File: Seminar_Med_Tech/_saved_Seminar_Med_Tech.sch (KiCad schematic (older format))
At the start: 72 parts, among them J1 CONN_02X08, U1 JP22, U10 JP31, U11 JP32, U12 JP33, U13 JP34, U14 J5, U15 JP35, U16 JP36, U17 JP37, U18 ADS1298, U19 OPA2340, U2 JP23, U20 ADS1298, U3 JP24, U4 JP25, U5 JP26, U6 JP27, U7 JP28, U8 JP29, U9 JP30

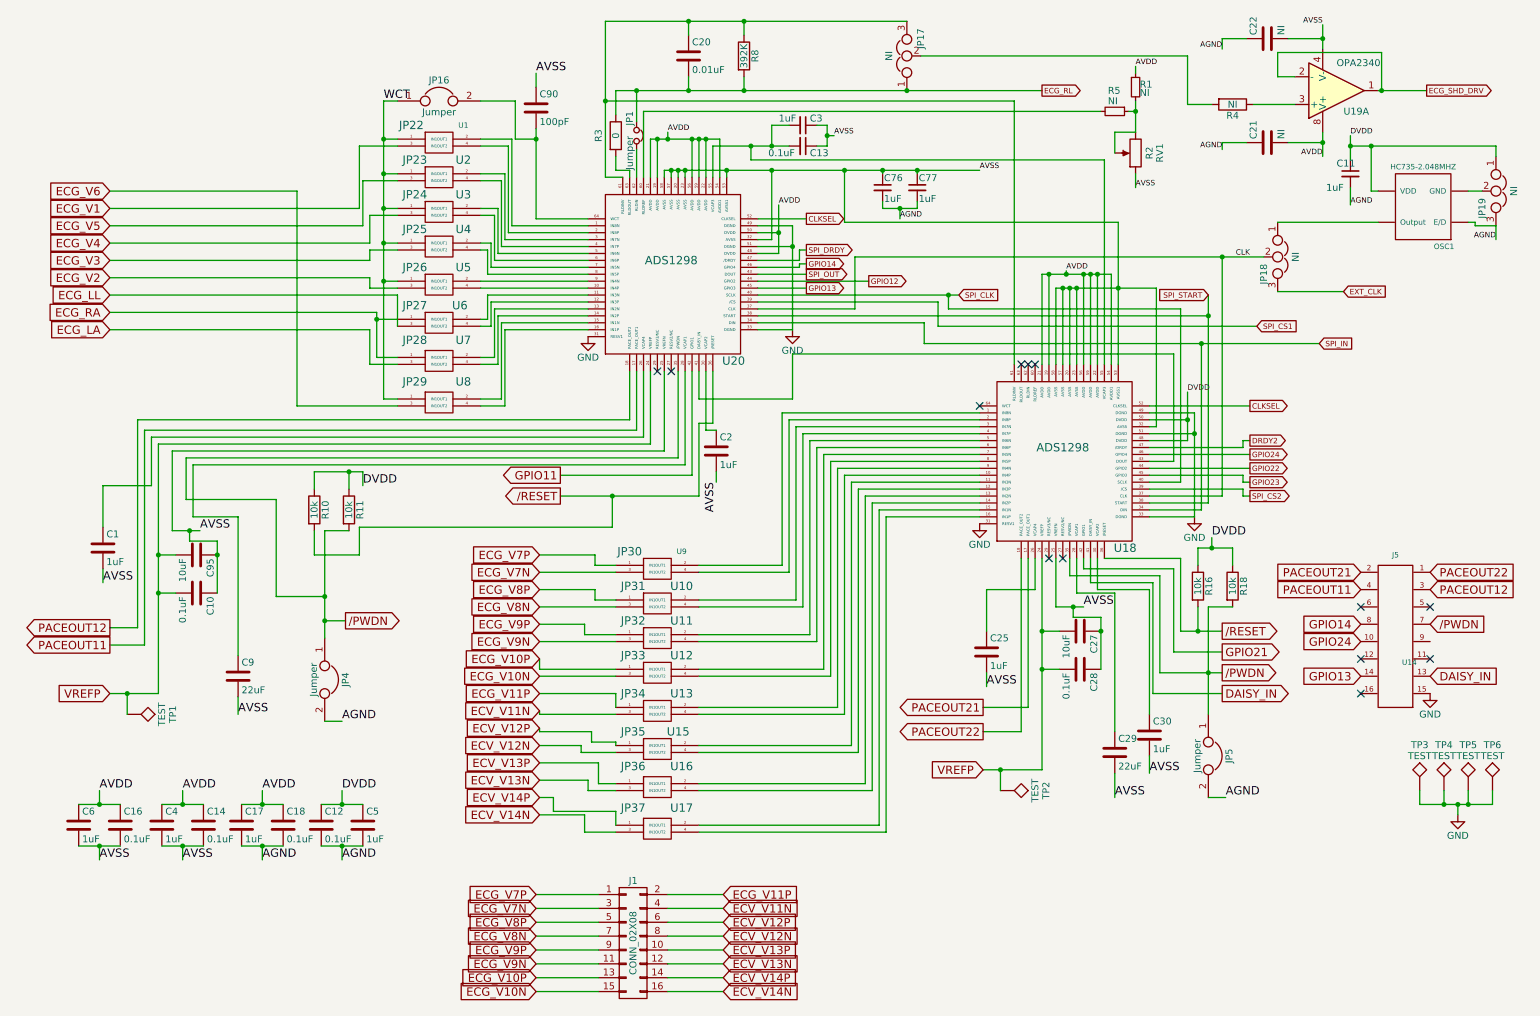
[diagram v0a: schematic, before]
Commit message: Changed labels
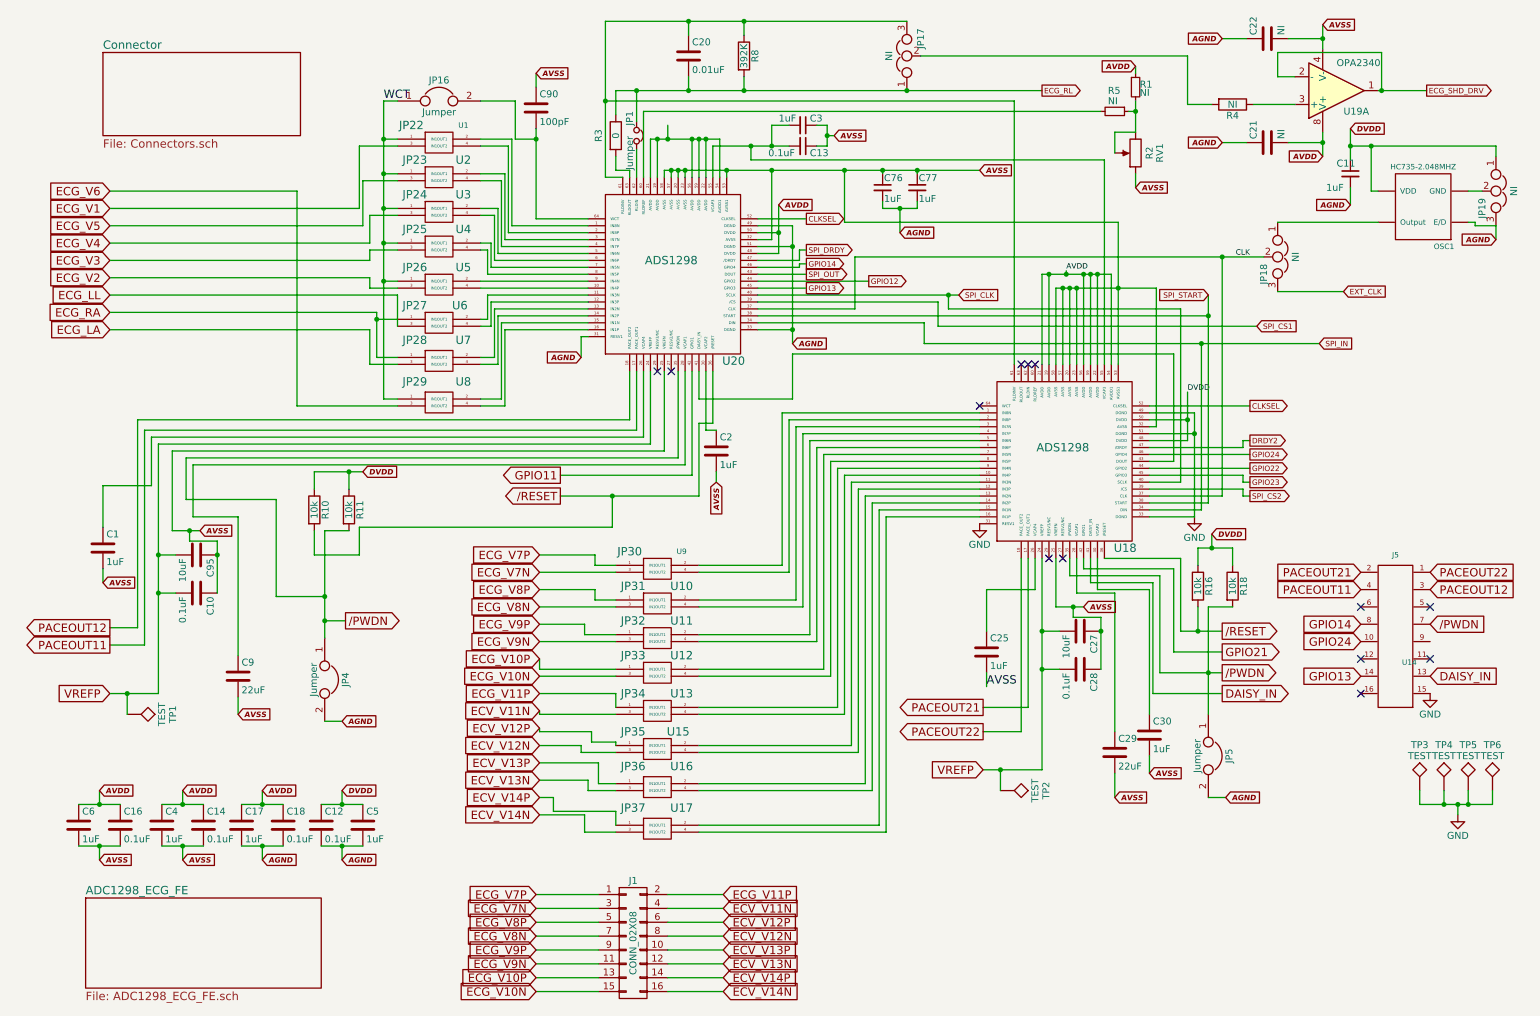
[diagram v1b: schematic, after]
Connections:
- net AGND: now also U20.31 (RESV1), U20.33 (DGND), U20.49 (DGND), U20.51 (DGND)
- net AVDD: no longer U20.19 (AVDD), U20.21 (AVDD), U20.22 (AVDD), U20.54 (AVDD1), U20.56 (AVDD), U20.59 (AVDD)
- net GND: no longer U20.31 (RESV1), U20.33 (DGND), U20.49 (DGND), U20.51 (DGND)
- new net: U20.19 (AVDD), U20.21 (AVDD), U20.22 (AVDD), U20.54 (AVDD1), U20.56 (AVDD), U20.59 (AVDD)
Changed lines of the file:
@@
 $Descr A4 11693 8268
 encoding utf-8
-Sheet 1 1
+Sheet 1 3
 Title ""
 Date ""
@@
 	1    0    0    -1
 $EndComp
-Text Label 4150 975  0    60   ~ 0
-AVSS
 $Comp
 L ADS1298 U20
@@
 Text Label 9300 2300 2    39   ~ 0
 CLK
-$Comp
-L GND #PWR02
-U 1 1 592AF0AE
-P 4525 2875
-F 0 "#PWR02" H 4525 2625 50  0001 C CNN
-F 1 "GND" H 4525 2725 50  0000 C CNN
-F 2 "" H 4525 2875 50  0001 C CNN
-F 3 "" H 4525 2875 50  0001 C CNN
-	1    4525 2875
-	1    0    0    -1
-$EndComp
 Text GLabel 7375 6000 0    60   Input ~ 0
 VREFP
@@
 	0    1    1    0
 $EndComp
-Text Label 9025 4325 0    60   ~ 0
-DVDD
 $Comp
 L C C30
@@
 	1    0    0    -1
 $EndComp
-Text Label 8575 6025 0    60   ~ 0
-AVSS
 $Comp
 L C C29
@@
 	1    0    0    -1
 $EndComp
-Text Label 8325 6200 0    60   ~ 0
-AVSS
 $Comp
 L C C25
@@
 $EndComp
 Text Label 7400 5400 0    60   ~ 0
-AVSS
-Text Label 8100 4825 0    60   ~ 0
 AVSS
 $Comp
@@
 	1    0    0    -1
 $EndComp
-Text Label 5450 3925 3    60   ~ 0
-AVSS
 $Comp
 L C C9
@@
 	1    0    0    -1
 $EndComp
-Text Label 2000 5600 0    60   ~ 0
-AVSS
 $Comp
 L C C1
@@
 	1    0    0    -1
 $EndComp
-Text Label 1025 4650 0    60   ~ 0
-AVSS
-Text Label 1725 4275 0    60   ~ 0
-AVSS
 $Comp
 L TEST TP1
@@
 	0    1    1    0
 $EndComp
-Text Label 2900 3950 0    60   ~ 0
-DVDD
 NoConn ~ 5025 3125
 NoConn ~ 5125 3125
 NoConn ~ 7350 3375
-$Comp
-L GND #PWR03
-U 1 1 592C9248
-P 6000 2825
-F 0 "#PWR03" H 6000 2575 50  0001 C CNN
-F 1 "GND" H 6000 2675 50  0000 C CNN
-F 2 "" H 6000 2825 50  0001 C CNN
-F 3 "" H 6000 2825 50  0001 C CNN
-	1    6000 2825
-	1    0    0    -1
-$EndComp
 $Comp
 L GND #PWR04
@@
 	1    0    0    -1
 $EndComp
-Text Label 1000 6150 0    60   ~ 0
-AVDD
-Text Label 1000 6650 0    60   ~ 0
-AVSS
 $Comp
 L C C4
@@
 	1    0    0    -1
 $EndComp
-Text Label 1600 6150 0    60   ~ 0
-AVDD
-Text Label 1600 6650 0    60   ~ 0
-AVSS
 $Comp
 L C C17
@@
 	1    0    0    -1
 $EndComp
-Text Label 2175 6150 0    60   ~ 0
-AVDD
-Text Label 2175 6650 0    60   ~ 0
-AGND
 $Comp
 L C C12
@@
 	1    0    0    -1
 $EndComp
-Text Label 2750 6150 0    60   ~ 0
-DVDD
-Text Label 2750 6650 0    60   ~ 0
-AGND
 $Comp
 L OPA2340 U19
@@
 	1    0    0    1
 $EndComp
-Text Label 9825 1575 2    39   ~ 0
-AVDD
 $Comp
 L C C21
@@
 	0    -1   -1   0
 $EndComp
-Text Label 9100 1525 2    39   ~ 0
-AGND
-Text Label 9825 625  2    39   ~ 0
-AVSS
 $Comp
 L C C22
@@
 Text GLabel 10575 1100 2    39   Output ~ 0
 ECG_SHD_DRV
-Text Label 9100 800  2    39   ~ 0
-AGND
 $Comp
 L R R4
@@
 Text GLabel 7800 1100 2    39   Output ~ 0
 ECG_RL
-Text Label 5100 1400 0    39   ~ 0
-AVDD
 $Comp
 L C_Small C13
@@
 	0    1    1    0
 $EndComp
-Text Label 6300 1425 0    39   ~ 0
-AVSS
 $Comp
 L C_Small C76
@@
 	1    0    0    -1
 $EndComp
-Text Label 6775 2025 0    39   ~ 0
-AGND
-Text Label 7350 1675 0    39   ~ 0
-AVSS
 Text Label 7975 2400 0    39   ~ 0
 AVDD
@@
 	1    0    0    -1
 $EndComp
-Text Label 8475 925  0    39   ~ 0
-AVDD
-Text Label 8475 1800 0    39   ~ 0
-AVSS
 $Comp
 L Jumper_NC_Dual JP18
@@
 	0    1    1    0
 $EndComp
-Text Label 11075 2175 2    39   ~ 0
-AGND
 $Comp
 L C_Small C11
@@
 	1    0    0    -1
 $EndComp
-Text Label 10025 1425 0    39   ~ 0
-DVDD
-Text Label 10025 1925 0    39   ~ 0
-AGND
-Text Label 5900 1925 0    39   ~ 0
-AVDD
 Text Label 8850 3275 0    39   ~ 0
 DVDD
@@
 Text GLabel 5500 7600 2    60   Input ~ 0
 ECV_V14N
-Text Label 9125 6200 0    60   ~ 0
-AGND
 Text Label 3050 1175 0    60   ~ 0
 WCT
-Text Label 2750 5650 0    60   ~ 0
+$Sheet
+S 1025 825  1425 600
+U 59470A40
+F0 "Connector" 60
+F1 "Connectors.sch" 60
+$EndSheet
+$Sheet
+S 900  6925 1700 650
+U 59470E15
+F0 "ADC1298_ECG_FE" 60
+F1 "ADC1298_ECG_FE.sch" 60
+$EndSheet
+Text GLabel 9825 625  2    39   Input Italic 8
+AVSS
+Text GLabel 9100 725  0    39   Input Italic 8
 AGND
+Text GLabel 9100 1475 0    39   Input Italic 8
+AGND
+Text GLabel 9825 1575 0    39   Input Italic 8
+AVDD
+Text GLabel 10025 1375 2    39   Input Italic 8
+DVDD
+Text GLabel 10025 1925 0    39   Input Italic 8
+AGND
+Text GLabel 11075 2175 0    39   Input Italic 8
+AGND
+Text GLabel 8475 1800 2    39   Input Italic 8
+AVSS
+Text GLabel 8475 925  0    39   Input Italic 8
+AVDD
+Text GLabel 6300 1425 2    39   Input Italic 8
+AVSS
+Text GLabel 7350 1675 2    39   Input Italic 8
+AVSS
+Text GLabel 6775 2125 2    39   Input Italic 8
+AGND
+Text GLabel 5900 1925 2    39   Input Italic 8
+AVDD
+Text GLabel 4150 975  2    39   Input Italic 8
+AVSS
+Text GLabel 4475 3025 0    39   Input Italic 8
+AGND
+Text GLabel 6000 2925 2    39   Input Italic 8
+AGND
+Text GLabel 2900 3850 2    39   Input Italic 8
+DVDD
+Text GLabel 1725 4275 2    39   Input Italic 8
+AVSS
+Text GLabel 1025 4650 2    39   Input Italic 8
+AVSS
+Text GLabel 5450 3925 3    39   Input Italic 8
+AVSS
+Text GLabel 2000 5600 2    39   Input Italic 8
+AVSS
+Text GLabel 2750 5650 2    39   Input Italic 8
+AGND
+Text GLabel 9025 4300 2    39   Input Italic 8
+DVDD
 Connection ~ 3000 2750
 Connection ~ 4150 1450
@@
 	9000 6200 9125 6200
 Wire Wire Line
-	9025 4325 9025 4400
+	9025 4300 9025 4400
 Connection ~ 9025 4400
 Wire Wire Line
@@
 Wire Wire Line
 	2550 3850 2900 3850
-Wire Wire Line
-	2900 3850 2900 3950
 Connection ~ 2800 3850
 Wire Wire Line
@@
 Connection ~ 9825 725
 Wire Wire Line
-	9275 725  9100 725
-Wire Wire Line
-	9100 725  9100 800
-Wire Wire Line
-	9275 1475 9100 1475
-Wire Wire Line
-	9100 1475 9100 1525
+	9100 725  9275 725
+Wire Wire Line
+	9100 1475 9275 1475
 Wire Wire Line
 	9625 1200 9325 1200
@@
 Connection ~ 5025 1450
 Wire Wire Line
-	5100 1450 5100 1400
+	5100 1350 5100 1450
 Connection ~ 5100 1450
 Wire Wire Line
@@
 	6900 1950 6900 1900
 Wire Wire Line
-	6775 1950 6775 2025
+	6775 1950 6775 2125
 Connection ~ 6775 1950
 Wire Wire Line
@@
 Connection ~ 10175 1500
 Wire Wire Line
-	10025 1425 10025 1600
+	10025 1375 10025 1600
 Wire Wire Line
 	10025 1800 10025 1925
@@
 	5750 2075 6000 2075
 Wire Wire Line
-	6000 2075 6000 2825
+	6000 2075 6000 2925
 Wire Wire Line
 	6000 2825 5750 2825
@@
 Wire Wire Line
 	2550 4450 2875 4450
+Wire Wire Line
+	4525 2875 4475 2875
+Wire Wire Line
+	4475 2875 4475 3025
+Connection ~ 6000 2825
+Text GLabel 8100 4825 2    39   Input Italic 8
+AVSS
+Text GLabel 9125 6200 2    39   Input Italic 8
+AGND
+Text GLabel 8325 6200 2    39   Input Italic 8
+AVSS
+Text GLabel 8575 6025 2    39   Input Italic 8
+AVSS
+Text GLabel 2750 6150 2    39   Input Italic 8
+DVDD
+Text GLabel 2750 6650 2    39   Input Italic 8
+AGND
+Text GLabel 2175 6650 2    39   Input Italic 8
+AGND
+Text GLabel 2175 6150 2    39   Input Italic 8
+AVDD
+Text GLabel 1600 6150 2    39   Input Italic 8
+AVDD
+Text GLabel 1000 6150 2    39   Input Italic 8
+AVDD
+Text GLabel 1600 6650 2    39   Input Italic 8
+AVSS
+Text GLabel 1000 6650 2    39   Input Italic 8
+AVSS
 $EndSCHEMATC
